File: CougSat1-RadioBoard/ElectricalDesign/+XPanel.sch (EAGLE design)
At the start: 63 parts, among them J1 ADCS Connector, J2 Low Gain +, J3 Low Gain -, J4 Low Gain Coax, J5 GPS Coax, J6 EPS Connector, U1 AD8515, U3 AD7291

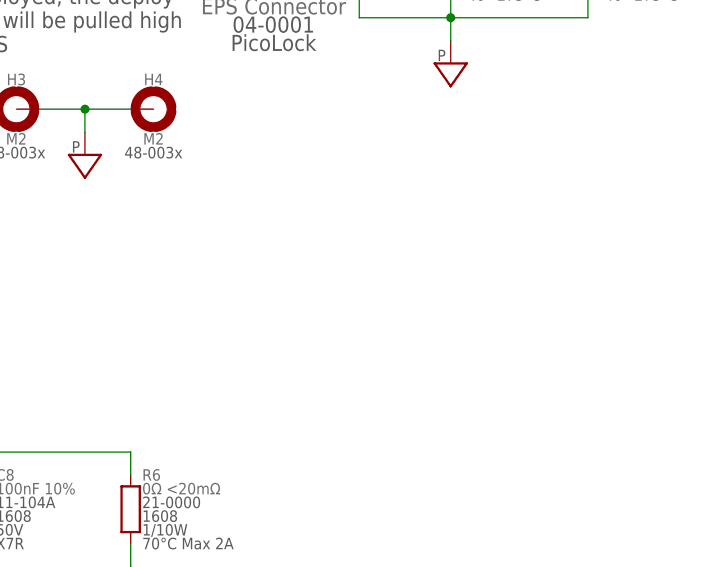
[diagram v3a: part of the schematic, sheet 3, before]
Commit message: Added Nuts
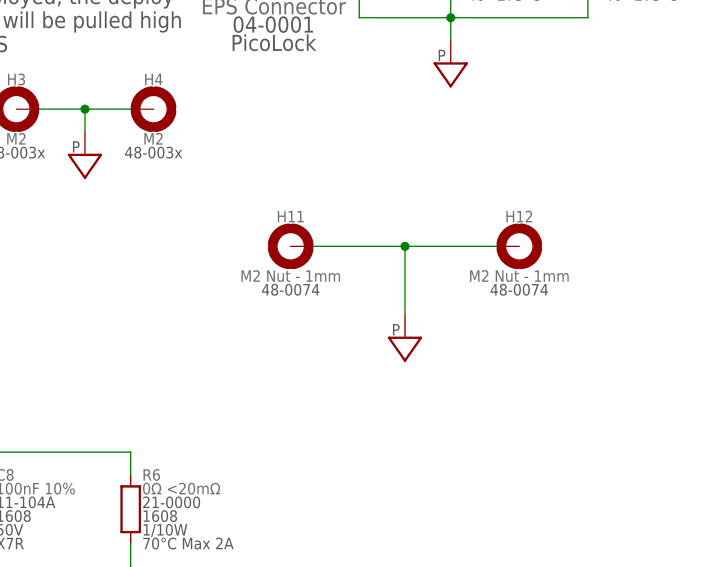
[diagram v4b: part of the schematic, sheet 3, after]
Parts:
- added H11, H12: M2 Nut - 1mm, CougsInSpace-Hardware:MOUNTING_HOLE-1MM-M2_NUT
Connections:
- net PGND: now also H11.MOUNT, H12.MOUNT
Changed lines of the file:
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@@
 <part name="SUPPLY55" library="CougsInSpace-PowerSymbols" deviceset="3.3V" device=""/>
 <part name="SUPPLY56" library="CougsInSpace-PowerSymbols" deviceset="3.3V" device=""/>
+<part name="H11" library="CougsInSpace-Hardware" deviceset="MOUNTING_HOLE" device="-M2_NUT" technology="-1MM" value="M2 Nut - 1mm"/>
+<part name="H12" library="CougsInSpace-Hardware" deviceset="MOUNTING_HOLE" device="-M2_NUT" technology="-1MM" value="M2 Nut - 1mm"/>
+<part name="SUPPLY57" library="CougsInSpace-PowerSymbols" deviceset="PGND" device=""/>
 </parts>
 <sheets>
@@
 <instance part="SUPPLY51" gate="G$1" x="162.56" y="66.04" smashed="yes"/>
 <instance part="SUPPLY52" gate="G$1" x="175.26" y="142.24" smashed="yes"/>
+<instance part="H11" gate="G$1" x="198.12" y="132.08" smashed="yes" rot="MR0">
+<attribute name="NAME" x="198.12" y="135.382" size="1.27" layer="95" rot="MR0" align="center"/>
+<attribute name="VALUE" x="198.12" y="128.778" size="1.27" layer="96" rot="MR0" align="center"/>
+<attribute name="SKU" x="198.12" y="127.254" size="1.27" layer="97" rot="MR0" align="center"/>
+</instance>
+<instance part="H12" gate="G$1" x="223.52" y="132.08" smashed="yes">
+<attribute name="NAME" x="223.52" y="135.382" size="1.27" layer="95" align="center"/>
+<attribute name="VALUE" x="223.52" y="128.778" size="1.27" layer="96" align="center"/>
+<attribute name="SKU" x="223.52" y="127.254" size="1.27" layer="97" align="center"/>
+</instance>
+<instance part="SUPPLY57" gate="G$1" x="210.82" y="121.92" smashed="yes"/>
 </instances>
 <busses>
@@
 <wire x1="180.34" y1="68.58" x2="180.34" y2="71.12" width="0.1524" layer="91"/>
 </segment>
-</net>
+<segment>
+<pinref part="H11" gate="G$1" pin="MOUNT"/>
+<wire x1="200.66" y1="132.08" x2="210.82" y2="132.08" width="0.1524" layer="91"/>
+<pinref part="SUPPLY57" gate="G$1" pin="PGND"/>
+<wire x1="210.82" y1="132.08" x2="210.82" y2="124.46" width="0.1524" layer="91"/>
+<pinref part="H12" gate="G$1" pin="MOUNT"/>
+<wire x1="210.82" y1="132.08" x2="220.98" y2="132.08" width="0.1524" layer="91"/>
+<junction x="210.82" y="132.08"/>
+</segment>
+</net>

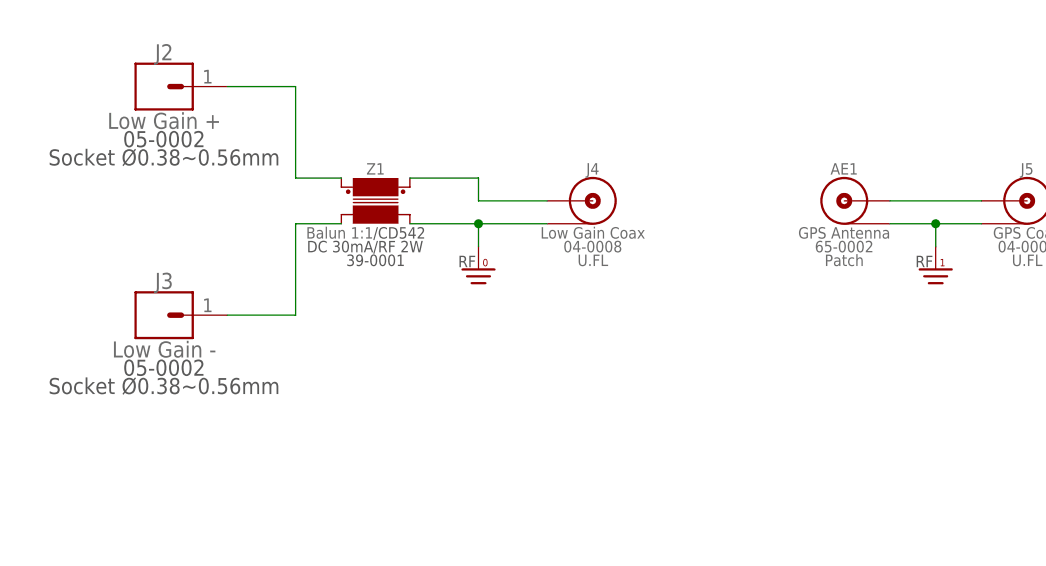
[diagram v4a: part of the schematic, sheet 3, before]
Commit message: Drew tKeepout for deployables
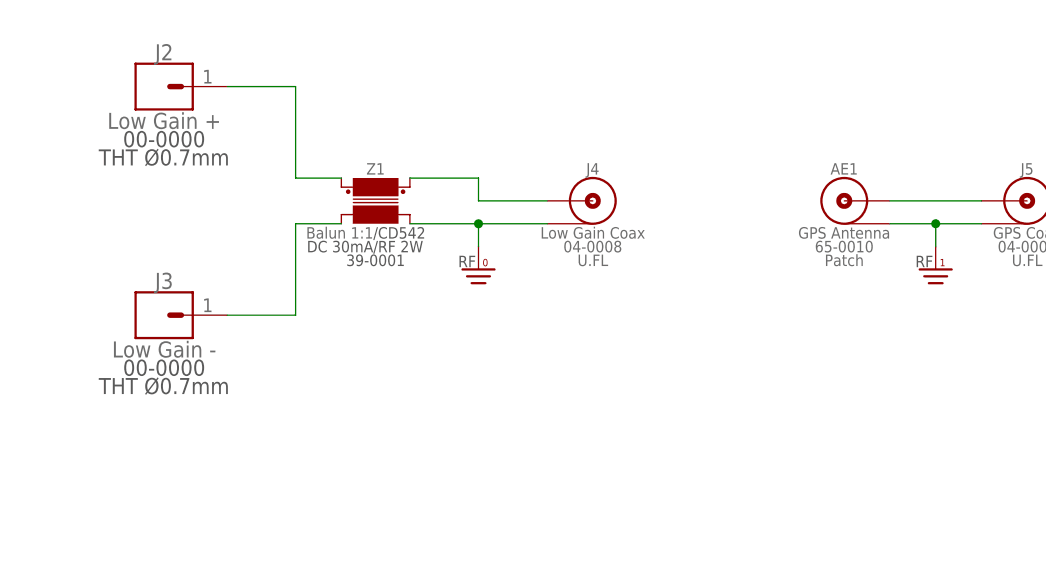
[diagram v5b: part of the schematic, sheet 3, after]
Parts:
- J2, J3: device CougsInSpace-Connectors:1X01-SOCKET-0.38~0.56MM -> CougsInSpace-Connectors:1X01-THT-0.7
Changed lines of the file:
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@@
 <?xml version="1.0" encoding="utf-8"?>
 <!DOCTYPE eagle SYSTEM "eagle.dtd">
-<eagle version="9.4.1">
+<eagle version="9.4.2">
 <drawing>
 <settings>
@@
 <setting verticaltext="up"/>
 </settings>
-<grid distance="0.1" unitdist="inch" unit="inch" style="lines" multiple="1" display="no" altdistance="0.05" altunitdist="inch" altunit="inch"/>
+<grid distance="0.1" unitdist="inch" unit="inch" style="lines" multiple="1" display="no" altdistance="0.01" altunitdist="inch" altunit="inch"/>
 <layers>
-<layer number="1" name="Top" color="4" fill="1" visible="no" active="no"/>
-<layer number="2" name="Route2" color="1" fill="3" visible="no" active="no"/>
-<layer number="3" name="Route3" color="4" fill="3" visible="no" active="no"/>
-<layer number="4" name="Route4" color="1" fill="4" visible="no" active="no"/>
-<layer number="5" name="Route5" color="4" fill="4" visible="no" active="no"/>
-<layer number="6" name="Route6" color="1" fill="8" visible="no" active="no"/>
-<layer number="7" name="Route7" color="4" fill="8" visible="no" active="no"/>
-<layer number="8" name="Route8" color="1" fill="2" visible="no" active="no"/>
-<layer number="9" name="Route9" color="4" fill="2" visible="no" active="no"/>
-<layer number="10" name="Route10" color="1" fill="7" visible="no" active="no"/>
-<layer number="11" name="Route11" color="4" fill="7" visible="no" active="no"/>
-<layer number="12" name="Route12" color="1" fill="5" visible="no" active="no"/>
-<layer number="13" name="Route13" color="4" fill="5" visible="no" active="no"/>
-<layer number="14" name="Route14" color="1" fill="6" visible="no" active="no"/>
-<layer number="15" name="Route15" color="4" fill="6" visible="no" active="no"/>
-<layer number="16" name="Bottom" color="1" fill="1" visible="no" active="no"/>
-<layer number="17" name="Pads" color="2" fill="1" visible="no" active="no"/>
-<layer number="18" name="Vias" color="2" fill="1" visible="no" active="no"/>
-<layer number="19" name="Unrouted" color="6" fill="1" visible="no" active="no"/>
-<layer number="20" name="Dimension" color="24" fill="1" visible="no" active="no"/>
-<layer number="21" name="tPlace" color="7" fill="1" visible="no" active="no"/>
-<layer number="22" name="bPlace" color="7" fill="1" visible="no" active="no"/>
-<layer number="23" name="tOrigins" color="15" fill="1" visible="no" active="no"/>
-<layer number="24" name="bOrigins" color="15" fill="1" visible="no" active="no"/>
-<layer number="25" name="tNames" color="7" fill="1" visible="no" active="no"/>
-<layer number="26" name="bNames" color="7" fill="1" visible="no" active="no"/>
-<layer number="27" name="tValues" color="7" fill="1" visible="no" active="no"/>
-<layer number="28" name="bValues" color="7" fill="1" visible="no" active="no"/>
+<layer number="1" name="Top" color="4" fill="1" visible="yes" active="no"/>
+<layer number="2" name="Route2" color="16" fill="1" visible="yes" active="no"/>
+<layer number="3" name="Route3" color="17" fill="1" visible="yes" active="no"/>
+<layer number="4" name="Route4" color="18" fill="1" visible="yes" active="no"/>
+<layer number="5" name="Route5" color="19" fill="1" visible="yes" active="no"/>
+<layer number="6" name="Route6" color="25" fill="1" visible="yes" active="no"/>
+<layer number="7" name="Route7" color="26" fill="1" visible="yes" active="no"/>
+<layer number="8" name="Route8" color="27" fill="1" visible="yes" active="no"/>
+<layer number="9" name="Route9" color="28" fill="1" visible="yes" active="no"/>
+<layer number="10" name="Route10" color="29" fill="1" visible="yes" active="no"/>
+<layer number="11" name="Route11" color="30" fill="1" visible="yes" active="no"/>
+<layer number="12" name="Route12" color="20" fill="1" visible="yes" active="no"/>
+<layer number="13" name="Route13" color="21" fill="1" visible="yes" active="no"/>
+<layer number="14" name="Route14" color="22" fill="1" visible="yes" active="no"/>
+<layer number="15" name="Route15" color="23" fill="1" visible="yes" active="no"/>
+<layer number="16" name="Bottom" color="1" fill="1" visible="yes" active="no"/>
+<layer number="17" name="Pads" color="2" fill="1" visible="yes" active="no"/>
+<layer number="18" name="Vias" color="2" fill="1" visible="yes" active="no"/>
+<layer number="19" name="Unrouted" color="6" fill="1" visible="yes" active="no"/>
+<layer number="20" name="Dimension" color="24" fill="1" visible="yes" active="no"/>
+<layer number="21" name="tPlace" color="7" fill="1" visible="yes" active="no"/>
+<layer number="22" name="bPlace" color="7" fill="1" visible="yes" active="no"/>
+<layer number="23" name="tOrigins" color="15" fill="1" visible="yes" active="no"/>
+<layer number="24" name="bOrigins" color="15" fill="1" visible="yes" active="no"/>
+<layer number="25" name="tNames" color="7" fill="1" visible="yes" active="no"/>
+<layer number="26" name="bNames" color="7" fill="1" visible="yes" active="no"/>
+<layer number="27" name="tValues" color="7" fill="1" visible="yes" active="no"/>
+<layer number="28" name="bValues" color="7" fill="1" visible="yes" active="no"/>
 <layer number="29" name="tStop" color="7" fill="3" visible="no" active="no"/>
 <layer number="30" name="bStop" color="7" fill="6" visible="no" active="no"/>
@@
 <layer number="35" name="tGlue" color="7" fill="4" visible="no" active="no"/>
 <layer number="36" name="bGlue" color="7" fill="5" visible="no" active="no"/>
-<layer number="37" name="tTest" color="7" fill="1" visible="no" active="no"/>
-<layer number="38" name="bTest" color="7" fill="1" visible="no" active="no"/>
+<layer number="37" name="tTest" color="7" fill="1" visible="yes" active="no"/>
+<layer number="38" name="bTest" color="7" fill="1" visible="yes" active="no"/>
 <layer number="39" name="tKeepout" color="4" fill="11" visible="no" active="no"/>
 <layer number="40" name="bKeepout" color="1" fill="11" visible="no" active="no"/>
@@
 <layer number="44" name="Drills" color="7" fill="1" visible="no" active="no"/>
 <layer number="45" name="Holes" color="7" fill="1" visible="no" active="no"/>
-<layer number="46" name="Milling" color="3" fill="1" visible="no" active="no"/>
-<layer number="47" name="Measures" color="7" fill="1" visible="no" active="no"/>
-<layer number="48" name="Document" color="7" fill="1" visible="no" active="no"/>
-<layer number="49" name="Reference" color="7" fill="1" visible="no" active="no"/>
-<layer number="50" name="dxf" color="7" fill="1" visible="no" active="no"/>
-<layer number="51" name="tDocu" color="7" fill="1" visible="no" active="no"/>
-<layer number="52" name="bDocu" color="7" fill="1" visible="no" active="no"/>
-<layer number="53" name="tGND_GNDA" color="7" fill="9" visible="no" active="no"/>
-<layer number="54" name="bGND_GNDA" color="1" fill="9" visible="no" active="no"/>
-<layer number="56" name="wert" color="7" fill="1" visible="no" active="no"/>
-<layer number="57" name="tCAD" color="7" fill="1" visible="no" active="no"/>
-<layer number="58" name="bCAD" color="9" fill="1" visible="no" active="no"/>
-<layer number="59" name="tCarbon" color="7" fill="1" visible="no" active="no"/>
-<layer number="60" name="bCarbon" color="7" fill="1" visible="no" active="no"/>
+<layer number="46" name="Milling" color="3" fill="1" visible="yes" active="no"/>
+<layer number="47" name="Measures" color="7" fill="1" visible="yes" active="no"/>
+<layer number="48" name="Document" color="7" fill="1" visible="yes" active="no"/>
+<layer number="49" name="Reference" color="7" fill="1" visible="yes" active="no"/>
+<layer number="50" name="dxf" color="7" fill="1" visible="yes" active="no"/>
+<layer number="51" name="tDocu" color="7" fill="1" visible="yes" active="no"/>
+<layer number="52" name="bDocu" color="7" fill="1" visible="yes" active="no"/>
+<layer number="53" name="tGND_GNDA" color="7" fill="9" visible="yes" active="no"/>
+<layer number="54" name="bGND_GNDA" color="1" fill="9" visible="yes" active="no"/>
+<layer number="56" name="wert" color="7" fill="1" visible="yes" active="no"/>
+<layer number="57" name="tCAD" color="7" fill="1" visible="yes" active="no"/>
+<layer number="58" name="bCAD" color="9" fill="1" visible="yes" active="no"/>
+<layer number="59" name="tCarbon" color="7" fill="1" visible="yes" active="no"/>
+<layer number="60" name="bCarbon" color="7" fill="1" visible="yes" active="no"/>
 <layer number="88" name="SimResults" color="9" fill="1" visible="yes" active="yes"/>
 <layer number="89" name="SimProbes" color="9" fill="1" visible="yes" active="yes"/>
@@
 <part name="SUPPLY14" library="CougsInSpace-PowerSymbols" deviceset="3.3V" device=""/>
 <part name="SUPPLY15" library="CougsInSpace-PowerSymbols" deviceset="PGND" device=""/>
-<part name="J2" library="CougsInSpace-Connectors" deviceset="1X01" device="-SOCKET-0.38~0.56MM" value="Low Gain +"/>
-<part name="J3" library="CougsInSpace-Connectors" deviceset="1X01" device="-SOCKET-0.38~0.56MM" value="Low Gain -"/>
+<part name="J2" library="CougsInSpace-Connectors" deviceset="1X01" device="-THT-0.7" value="Low Gain +"/>
+<part name="J3" library="CougsInSpace-Connectors" deviceset="1X01" device="-THT-0.7" value="Low Gain -"/>
 <part name="J4" library="CougsInSpace-Connectors" deviceset="COAX" device="-U.FL" value="Low Gain Coax"/>
 <part name="Z1" library="CougsInSpace-Coils" deviceset="BALUN" device="-CD542" technology="-ADTL1-12+" value="Balun 1:1"/>

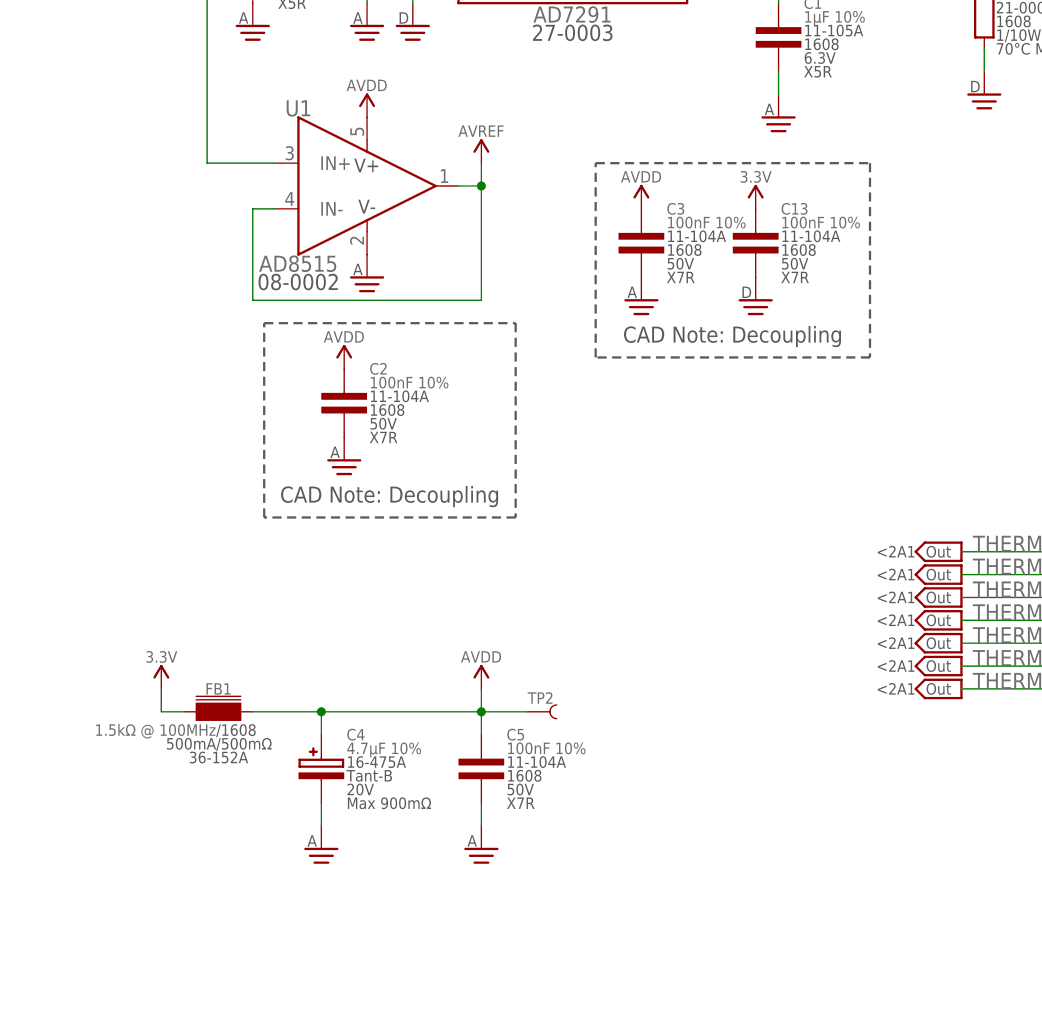
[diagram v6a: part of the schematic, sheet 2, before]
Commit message: Moved decoupling capacitors
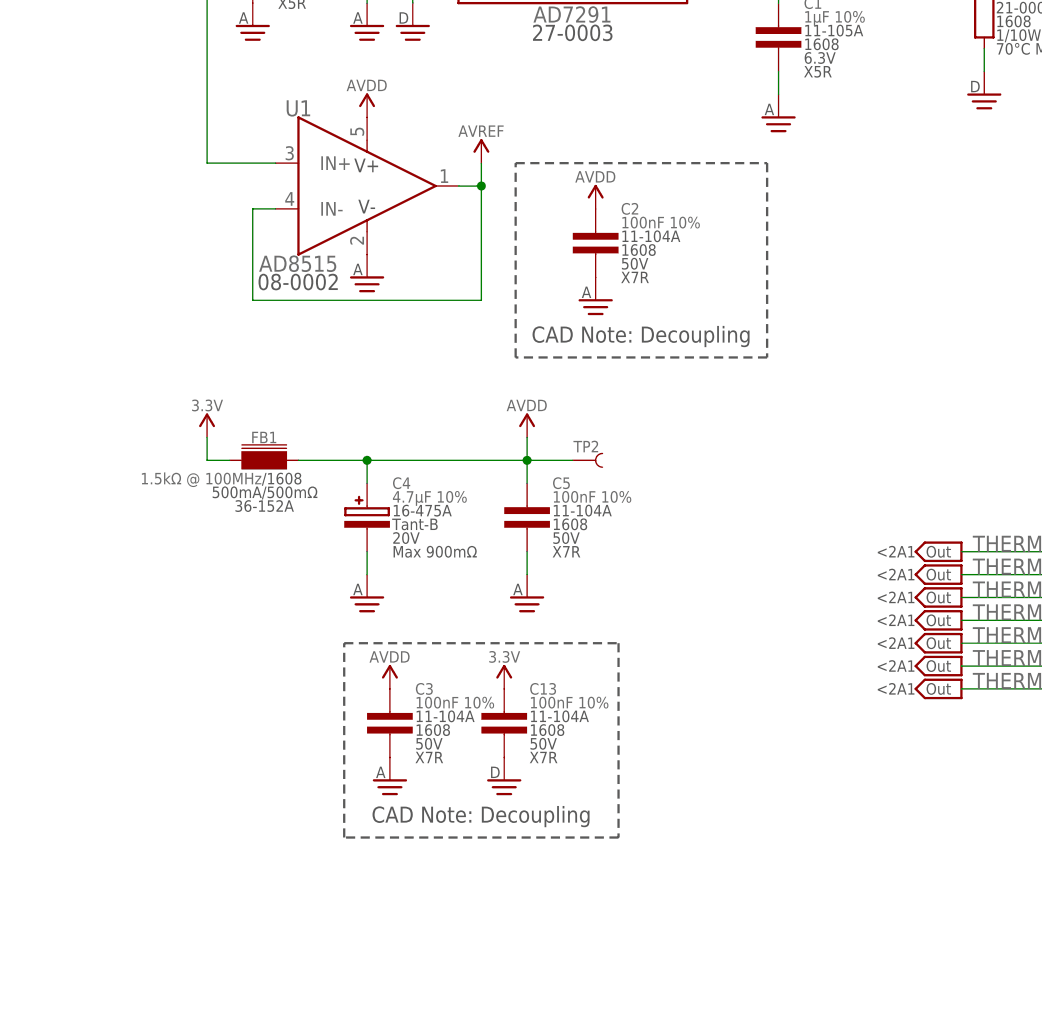
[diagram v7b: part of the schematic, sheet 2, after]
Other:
- moved on the sheet: C13, C2, C3, C4, C5, FB1, TP2
